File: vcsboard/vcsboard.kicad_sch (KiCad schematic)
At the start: 23 parts, among them J1 Vcc / C53, J2 Video / R56, J3 Audio / C49, J4 Conn_01x06_Male, J5 Ground, Q4 2N2222A, U1 CD4053B

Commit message: add part description for more complex parts, remove unused cap
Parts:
- removed C1: 100nF, Capacitor_SMD:C_1206_3216Metric_Pad1.33x1.80mm_HandSolder, symbol Device:C_Small
- J4: Part (none) -> Amtek 2542R-06TW-L; Part (Alt 1) (none) -> JST like JH2.54-6 (Part of X0014J7UB1)
- Q4: Part (none) -> Nexperia PMBT2222A
- U1: Part (none) -> Texas Instruments CD4053BM
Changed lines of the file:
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@@
     (rev "C")
   )
-  (junction (at 66.04 83.82) (diameter 0) (color 0 0 0 0)
-  )
   (junction (at 130.81 113.03) (diameter 0) (color 0 0 0 0)
   )
@@
   (junction (at 142.24 152.4) (diameter 0) (color 0 0 0 0)
   )
-  (junction (at 43.18 83.82) (diameter 0) (color 0 0 0 0)
-  )
   (junction (at 60.96 128.27) (diameter 0) (color 0 0 0 0)
   )
@@
     (stroke (width 0) (type default) (color 0 0 0 0))
   )
-  (wire (pts (xy 43.18 83.82) (xy 43.18 95.25))
-    (stroke (width 0) (type default) (color 0 0 0 0))
-  )
   (wire (pts (xy 130.81 113.03) (xy 130.81 102.87))
     (stroke (width 0) (type default) (color 0 0 0 0))
@@
     (stroke (width 0) (type default) (color 0 0 0 0))
   )
-  (wire (pts (xy 43.18 76.2) (xy 43.18 83.82))
+  (wire (pts (xy 43.18 76.2) (xy 43.18 95.25))
     (stroke (width 0) (type default) (color 0 0 0 0))
   )
@@
     (stroke (width 0) (type default) (color 0 0 0 0))
   )
-  (wire (pts (xy 43.18 83.82) (xy 50.8 83.82))
-    (stroke (width 0) (type default) (color 0 0 0 0))
-  )
   (wire (pts (xy 63.5 152.4) (xy 107.95 152.4))
     (stroke (width 0) (type default) (color 0 0 0 0))
@@
   )
   (wire (pts (xy 107.95 129.54) (xy 107.95 144.78))
-    (stroke (width 0) (type default) (color 0 0 0 0))
-  )
-  (wire (pts (xy 55.88 83.82) (xy 66.04 83.82))
     (stroke (width 0) (type default) (color 0 0 0 0))
   )
@@
       (effects (font (size 1.27 1.27)) hide)
     )
+    (property "Part" "Nexperia PMBT2222A" (id 4) (at 128.27 97.79 0)
+      (effects (font (size 1.27 1.27)) hide)
+    )
     (pin "1")
     (pin "2")
@@
       (effects (font (size 1.27 1.27)) hide)
     )
+    (property "Part" "Amtek 2542R-06TW-L" (id 4) (at 162.56 124.46 0)
+      (effects (font (size 1.27 1.27)) hide)
+    )
+    (property "Part (Alt 1)" "JST like JH2.54-6 (Part of X0014J7UB1)" (id 5) (at 162.56 124.46 0)
+      (effects (font (size 1.27 1.27)) hide)
+    )
     (pin "1")
     (pin "2")
@@
     (pin "6")
   )
-  (symbol (lib_id "Device:C_Small") (at 53.34 83.82 90) (mirror x) (unit 1)
-    (in_bom yes) (on_board yes)
-    (property "Reference" "C1" (id 0) (at 53.34 78.74 90))
-    (property "Value" "100nF" (id 1) (at 54.61 81.28 90))
-    (property "Footprint" "Capacitor_SMD:C_1206_3216Metric_Pad1.33x1.80mm_HandSolder" (id 2) (at 53.34 83.82 0)
-      (effects (font (size 1.27 1.27)) hide)
-    )
-    (property "Datasheet" "~" (id 3) (at 53.34 83.82 0)
-      (effects (font (size 1.27 1.27)) hide)
-    )
-    (pin "1")
-    (pin "2")
-  )
   (symbol (lib_id "Device:C_Small") (at 142.24 97.79 0) (unit 1)
     (in_bom yes) (on_board yes) (fields_autoplaced)
@@
     )
     (property "Datasheet" "http://www.ti.com/lit/ds/symlink/cd4052b.pdf" (id 3) (at 62.992 102.87 0)
+      (effects (font (size 1.27 1.27)) hide)
+    )
+    (property "Part" "Texas Instruments CD4053BM" (id 4) (at 63.5 107.95 0)
       (effects (font (size 1.27 1.27)) hide)
     )
@@
       (reference "#PWR0102") (unit 1) (value "GNDD") (footprint "")
     )
-    (path "/bbe5c3ff-109d-40b9-8bb3-c0feeb56f393"
-      (reference "C1") (unit 1) (value "100nF") (footprint "Capacitor_SMD:C_1206_3216Metric_Pad1.33x1.80mm_HandSolder")
-    )
     (path "/0062b5da-0373-4ea1-afe0-05303d5a4416"

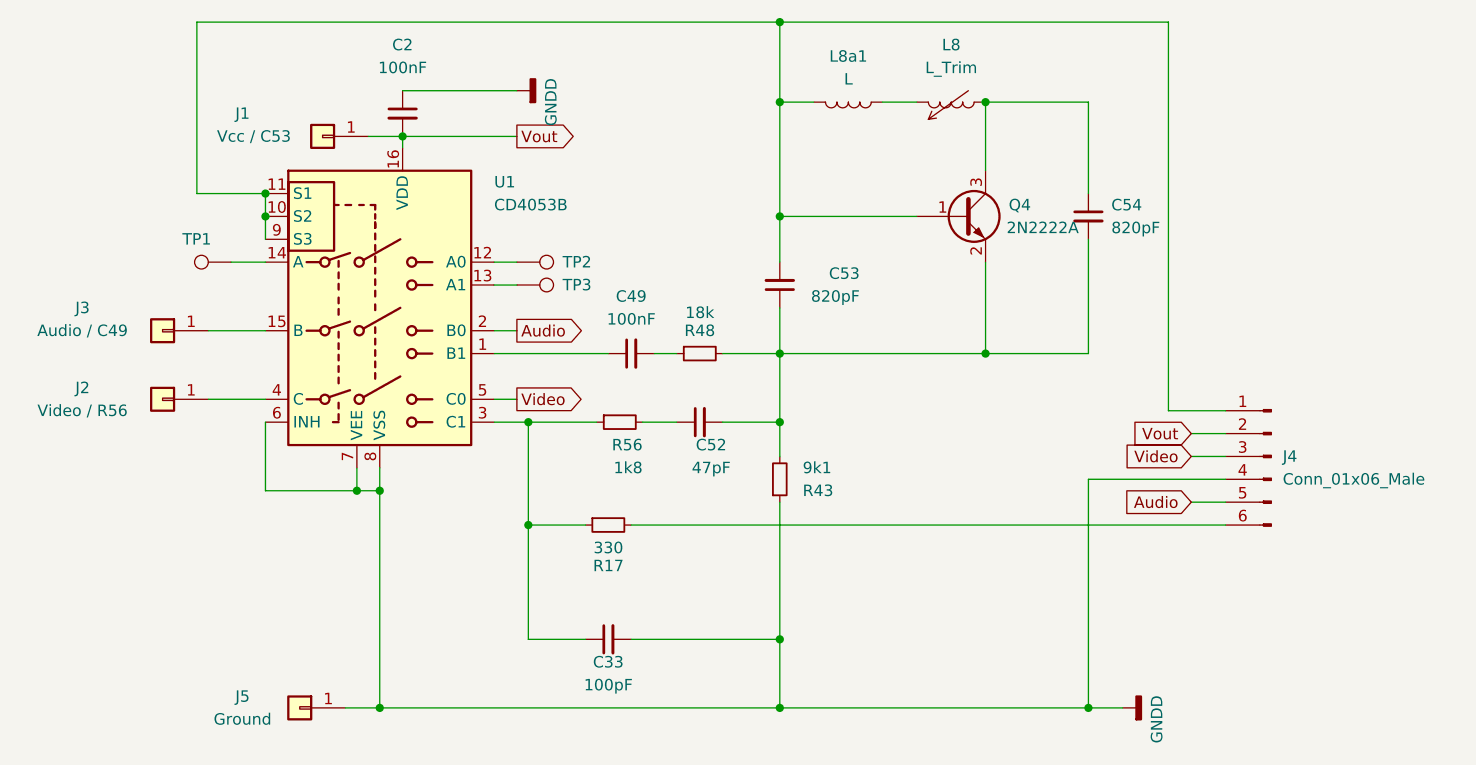
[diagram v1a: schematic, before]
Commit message: add some more parts, use 0805 components for C53 & C54
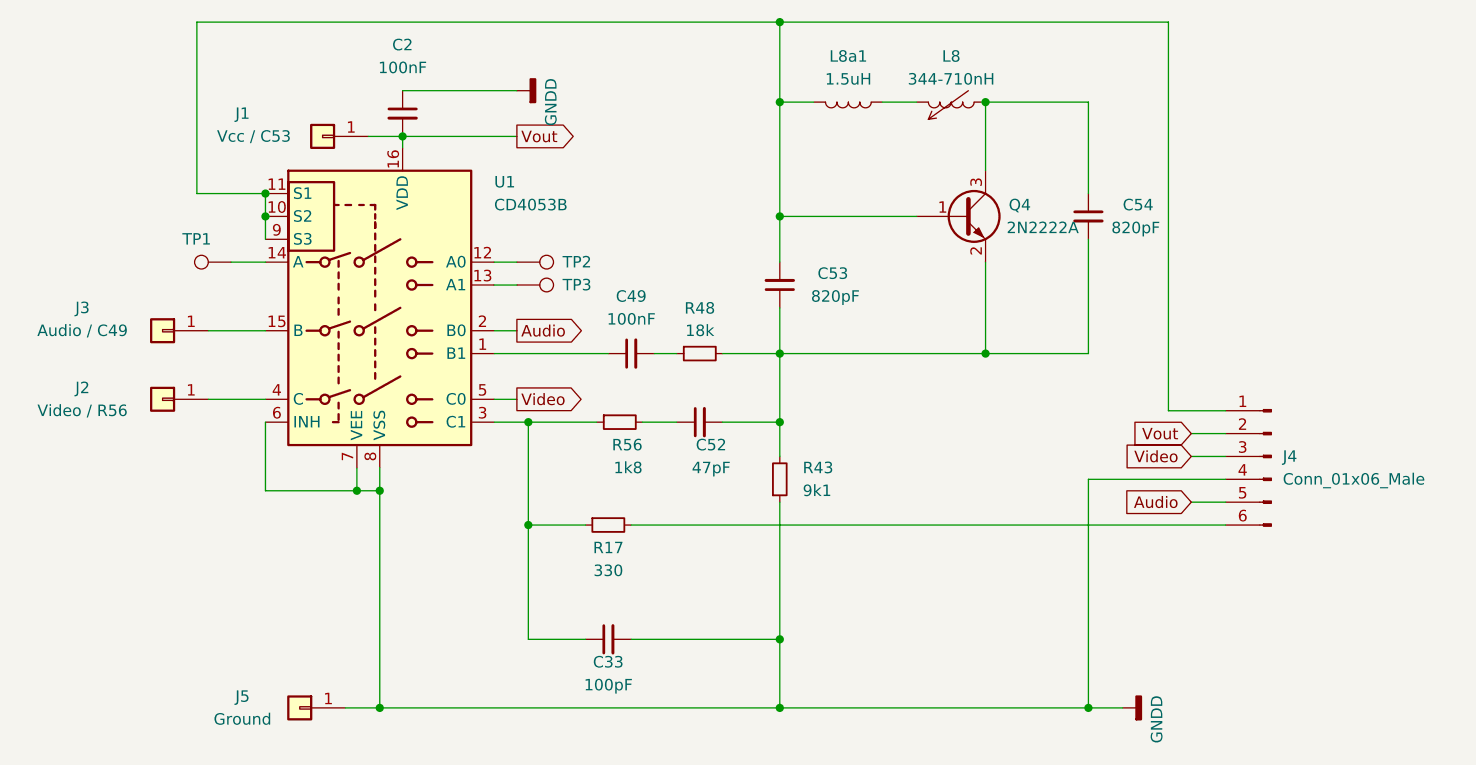
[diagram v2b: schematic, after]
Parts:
- C2, C49: Part (none) -> Yageo CC1206KRX7R9BB104
- C33: Part (none) -> Yageo CC1206JRNPO9BN101
- C52: Part (none) -> Yageo CC1206JRNPO9BN470
- C53, C54: footprint Capacitor_SMD:C_1206_3216Metric_Pad1.33x1.80mm_HandSolder -> Capacitor_SMD:C_0805_2012Metric_Pad1.18x1.45mm_HandSolder; Part (none) -> Panasonic ECH-U1H821GX5
- J2: Part (none) -> MPE Garry 087-1-004
- L8: value L_Trim -> 344-710nH; Part (none) -> Coilcraft 148-13J12L
- L8a1: value L -> 1.5uH; Part (none) -> TDK TFM201210ALMA1R5MTAA
- R17: Part (none) -> Yageo RC1206JR-07330RL
- R43: Part (none) -> Yageo RC1206JR-079K1L
- R48: Part (none) -> Yageo RC1206JR-0718KL
- R56: Part (none) -> Yageo RC1206JR-071K8L
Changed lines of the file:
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@@
+      (effects (font (size 1.27 1.27)) hide)
+    )
+    (property "Part" "Yageo CC1206KRX7R9BB104" (id 4) (at 66.04 86.36 0)
       (effects (font (size 1.27 1.27)) hide)
     )
@@
   )
   (symbol (lib_id "Device:L_Trim") (at 127 85.09 90) (mirror x) (unit 1)
-    (in_bom yes) (on_board yes) (fields_autoplaced)
-    (property "Reference" "L8" (id 0) (at 127 78.74 90))
-    (property "Value" "L_Trim" (id 1) (at 127 81.28 90))
+    (in_bom yes) (on_board yes)
+    (property "Reference" "L8" (id 0) (at 127 80.01 90))
+    (property "Value" "344-710nH" (id 1) (at 127 82.55 90))
     (property "Footprint" "vcsboard:tim_laying" (id 2) (at 127 85.09 0)
       (effects (font (size 1.27 1.27)) hide)
     )
     (property "Datasheet" "~" (id 3) (at 127 85.09 0)
+      (effects (font (size 1.27 1.27)) hide)
+    )
+    (property "Part" "Coilcraft 148-13J12L" (id 4) (at 127 85.09 90)
       (effects (font (size 1.27 1.27)) hide)
     )
@@
   (symbol (lib_name "R_Small_1") (lib_id "Device:R_Small") (at 99.06 113.03 90) (mirror x) (unit 1)
     (in_bom yes) (on_board yes)
-    (property "Reference" "R48" (id 0) (at 99.06 110.49 90))
-    (property "Value" "18k" (id 1) (at 99.06 108.49 90))
+    (property "Reference" "R48" (id 0) (at 99.06 108 90))
+    (property "Value" "18k" (id 1) (at 99.06 110.49 90))
     (property "Footprint" "Resistor_SMD:R_1206_3216Metric_Pad1.30x1.75mm_HandSolder" (id 2) (at 99.06 113.03 0)
       (effects (font (size 1.27 1.27)) hide)
@@
       (effects (font (size 1.27 1.27)) hide)
     )
+    (property "Part" "Yageo RC1206JR-0718KL" (id 4) (at 99.06 113.03 90)
+      (effects (font (size 1.27 1.27)) hide)
+    )
     (pin "1")
     (pin "2")
@@
   (symbol (lib_id "Device:R_Small") (at 107.95 127 0) (mirror x) (unit 1)
     (in_bom yes) (on_board yes)
-    (property "Reference" "R43" (id 0) (at 110.49 128.2701 0)
-      (effects (font (size 1.27 1.27)) (justify left))
-    )
-    (property "Value" "9k1" (id 1) (at 110.49 125.7301 0)
+    (property "Reference" "R43" (id 0) (at 110.49 125.73 0)
+      (effects (font (size 1.27 1.27)) (justify left))
+    )
+    (property "Value" "9k1" (id 1) (at 110.49 128.27 0)
       (effects (font (size 1.27 1.27)) (justify left))
     )
@@
     )
     (property "Datasheet" "~" (id 3) (at 107.95 127 0)
+      (effects (font (size 1.27 1.27)) hide)
+    )
+    (property "Part" "Yageo RC1206JR-079K1L" (id 4) (at 107.95 127 0)
       (effects (font (size 1.27 1.27)) hide)
     )
@@
       (effects (font (size 1.27 1.27)) hide)
     )
+    (property "Part" "Yageo CC1206KRX7R9BB104" (id 4) (at 91.44 113.03 90)
+      (effects (font (size 1.27 1.27)) hide)
+    )
     (pin "1")
     (pin "2")
@@
       (effects (font (size 1.27 1.27)) hide)
     )
+    (property "Part" "Yageo CC1206JRNPO9BN101" (id 4) (at 88.9 144.78 90)
+      (effects (font (size 1.27 1.27)) hide)
+    )
     (pin "1")
     (pin "2")
@@
   (symbol (lib_id "Device:C_Small") (at 107.95 105.41 0) (mirror x) (unit 1)
     (in_bom yes) (on_board yes)
-    (property "Reference" "C53" (id 0) (at 116.84 104.14 0)
+    (property "Reference" "C53" (id 0) (at 115.57 104.14 0)
       (effects (font (size 1.27 1.27)) (justify right))
     )
@@
       (effects (font (size 1.27 1.27)) (justify right))
     )
-    (property "Footprint" "Capacitor_SMD:C_1206_3216Metric_Pad1.33x1.80mm_HandSolder" (id 2) (at 107.95 105.41 0)
+    (property "Footprint" "Capacitor_SMD:C_0805_2012Metric_Pad1.18x1.45mm_HandSolder" (id 2) (at 107.95 105.41 0)
       (effects (font (size 1.27 1.27)) hide)
     )
     (property "Datasheet" "~" (id 3) (at 107.95 105.41 0)
+      (effects (font (size 1.27 1.27)) hide)
+    )
+    (property "Part" "Panasonic ECH-U1H821GX5" (id 4) (at 107.95 105.41 0)
       (effects (font (size 1.27 1.27)) hide)
     )
@@
   )
   (symbol (lib_id "Device:C_Small") (at 142.24 97.79 0) (unit 1)
-    (in_bom yes) (on_board yes) (fields_autoplaced)
-    (property "Reference" "C54" (id 0) (at 144.78 96.5262 0)
+    (in_bom yes) (on_board yes)
+    (property "Reference" "C54" (id 0) (at 146.05 96.52 0)
       (effects (font (size 1.27 1.27)) (justify left))
     )
@@
       (effects (font (size 1.27 1.27)) (justify left))
     )
-    (property "Footprint" "Capacitor_SMD:C_1206_3216Metric_Pad1.33x1.80mm_HandSolder" (id 2) (at 142.24 97.79 0)
+    (property "Footprint" "Capacitor_SMD:C_0805_2012Metric_Pad1.18x1.45mm_HandSolder" (id 2) (at 142.24 97.79 0)
       (effects (font (size 1.27 1.27)) hide)
     )
     (property "Datasheet" "~" (id 3) (at 142.24 97.79 0)
+      (effects (font (size 1.27 1.27)) hide)
+    )
+    (property "Part" "Panasonic ECH-U1H821GX5" (id 4) (at 142.24 97.79 0)
       (effects (font (size 1.27 1.27)) hide)
     )
@@
       (effects (font (size 1.27 1.27)) hide)
     )
+    (property "Part" "MPE Garry  087-1-004" (id 4) (at 39.37 118.11 0)
+      (effects (font (size 1.27 1.27)) hide)
+    )
     (pin "1")
   )
@@
     )
     (property "Datasheet" "~" (id 3) (at 99.06 120.65 0)
+      (effects (font (size 1.27 1.27)) hide)
+    )
+    (property "Part" "Yageo CC1206JRNPO9BN470" (id 4) (at 99.06 120.65 90)
       (effects (font (size 1.27 1.27)) hide)
     )
@@
   (symbol (lib_name "R_Small_1") (lib_id "Device:R_Small") (at 88.9 132.08 90) (mirror x) (unit 1)
     (in_bom yes) (on_board yes)
-    (property "Reference" "R17" (id 0) (at 88.9063 136.62 90))
-    (property "Value" "330" (id 1) (at 88.9063 134.62 90))
+    (property "Reference" "R17" (id 0) (at 88.9 134.62 90))
+    (property "Value" "330" (id 1) (at 88.9 137.16 90))
     (property "Footprint" "Resistor_SMD:R_1206_3216Metric_Pad1.30x1.75mm_HandSolder" (id 2) (at 88.9 132.08 0)
       (effects (font (size 1.27 1.27)) hide)
@@
       (effects (font (size 1.27 1.27)) hide)
     )
+    (property "Part" "Yageo RC1206JR-07330RL" (id 4) (at 88.9 132.08 90)
+      (effects (font (size 1.27 1.27)) hide)
+    )
     (pin "1")
     (pin "2")
@@
     )
     (property "Datasheet" "~" (id 3) (at 90.17 120.65 0)
+      (effects (font (size 1.27 1.27)) hide)
+    )
+    (property "Part" "Yageo RC1206JR-071K8L" (id 4) (at 90.17 120.65 90)
       (effects (font (size 1.27 1.27)) hide)
     )
@@
     (in_bom yes) (on_board yes) (fields_autoplaced)
     (property "Reference" "L8a1" (id 0) (at 115.57 80.01 90))
-    (property "Value" "L" (id 1) (at 115.57 82.55 90))
+    (property "Value" "1.5uH" (id 1) (at 115.57 82.55 90))
     (property "Footprint" "Inductor_SMD:L_0805_2012Metric_Pad1.05x1.20mm_HandSolder" (id 2) (at 115.57 85.09 0)
       (effects (font (size 1.27 1.27)) hide)
     )
     (property "Datasheet" "~" (id 3) (at 115.57 85.09 0)
+      (effects (font (size 1.27 1.27)) hide)
+    )
+    (property "Part" "TDK TFM201210ALMA1R5MTAA" (id 4) (at 115.57 85.09 90)
       (effects (font (size 1.27 1.27)) hide)
     )
@@
     )
     (path "/776e6552-c1e5-4c2d-8207-a238b5804c16"
-      (reference "C53") (unit 1) (value "820pF") (footprint "Capacitor_SMD:C_1206_3216Metric_Pad1.33x1.80mm_HandSolder")
+      (reference "C53") (unit 1) (value "820pF") (footprint "Capacitor_SMD:C_0805_2012Metric_Pad1.18x1.45mm_HandSolder")
     )
     (path "/c5aae5b6-549f-494a-9fbe-9764e6124274"
-      (reference "C54") (unit 1) (value "820pF") (footprint "Capacitor_SMD:C_1206_3216Metric_Pad1.33x1.80mm_HandSolder")
+      (reference "C54") (unit 1) (value "820pF") (footprint "Capacitor_SMD:C_0805_2012Metric_Pad1.18x1.45mm_HandSolder")
     )
     (path "/77c526ed-42d4-44a2-9b68-8d0aea50a043"
@@
     )
     (path "/13e40e47-ab73-4e00-9bc1-154a9734d157"
-      (reference "L8") (unit 1) (value "L_Trim") (footprint "vcsboard:tim_laying")
+      (reference "L8") (unit 1) (value "344-710nH") (footprint "vcsboard:tim_laying")
     )
     (path "/f743c59a-fd11-4ea9-b5f6-98751b020150"
-      (reference "L8a1") (unit 1) (value "L") (footprint "Inductor_SMD:L_0805_2012Metric_Pad1.05x1.20mm_HandSolder")
+      (reference "L8a1") (unit 1) (value "1.5uH") (footprint "Inductor_SMD:L_0805_2012Metric_Pad1.05x1.20mm_HandSolder")
     )
     (path "/9a7b5c17-79ff-46da-b447-1001d0c57627"

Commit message: add first draft of documentation, add another alternative
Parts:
- J2: Part (Alt 1) (none) -> Amphenol G800LW304032EU
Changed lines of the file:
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@@
+      (effects (font (size 1.27 1.27)) hide)
+    )
+    (property "Part (Alt 1)" "Amphenol G800LW304032EU" (id 5) (at 39.37 118.11 0)
       (effects (font (size 1.27 1.27)) hide)
     )

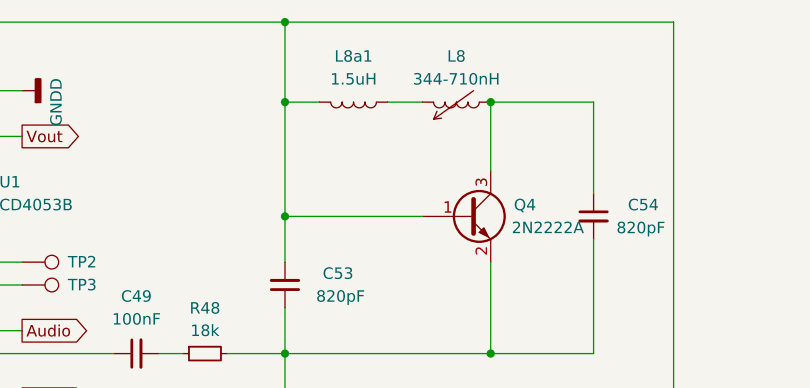
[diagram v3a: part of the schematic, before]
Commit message: update to Kicad 8
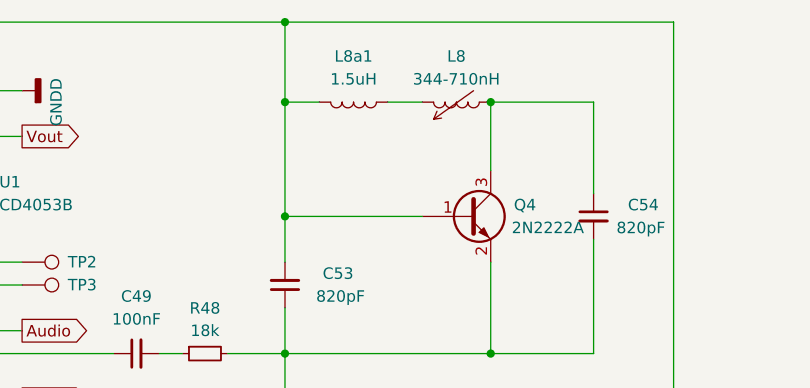
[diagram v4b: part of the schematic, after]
